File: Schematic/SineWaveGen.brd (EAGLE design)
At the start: 100 x 80 mm, 16 parts, among them IC1 MEGA32-P, Q1 G20N60, Q2 G20N60, Q3 H9NA80FI, Q4 H9NA80FI

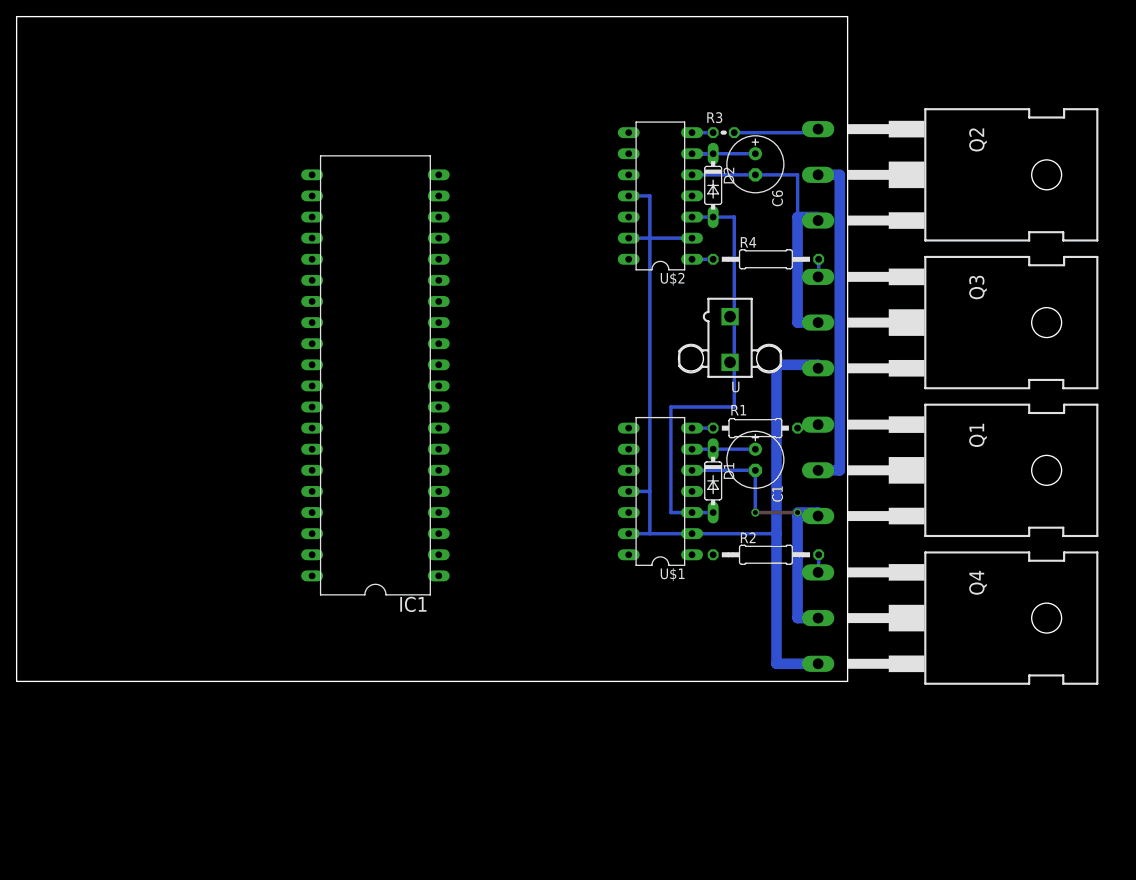
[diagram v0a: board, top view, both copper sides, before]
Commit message: use bigger distances for high voltages
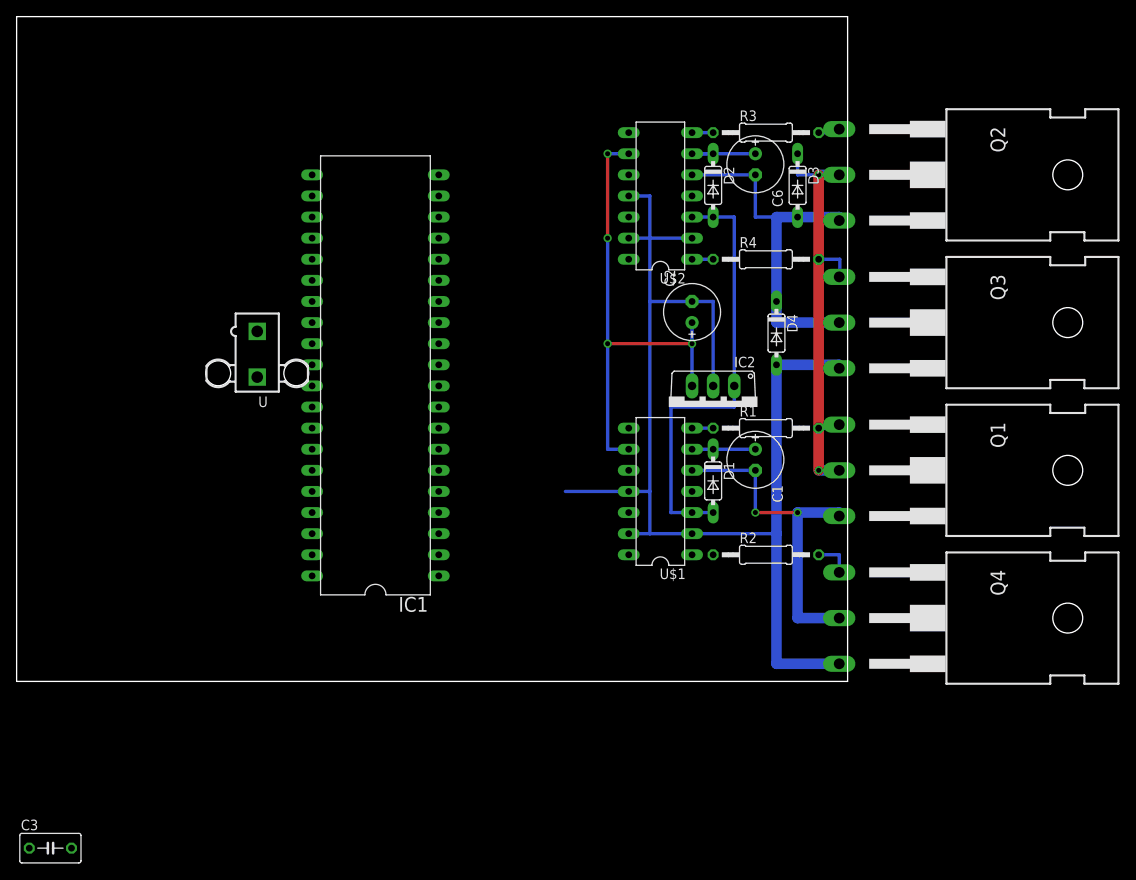
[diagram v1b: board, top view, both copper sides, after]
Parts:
- added C2: 100u, rcl:E2,5-7
- added C3: 100n, rcl:C050-035X075
- added D3, D4: 1N4148, diode:DO35-7
- added IC2: 7805TV, linear:TO220V
- Q1: value G20N60 -> (none)
- Q2: value G20N60 -> H9NA80FI
- Q4: value H9NA80FI -> (none)
- R1: device rcl:0207/10 -> rcl:0207/12
- R3: device rcl:0204V -> rcl:0207/12
- moved U 56.9 mm to (29.0, 39.4)
- moved R3 5.08 mm to (90.2, 66.0)
- moved Q1 2.54 mm to (126.5, 25.4)
- moved Q2 2.54 mm to (126.5, 61.0)
- moved Q3 2.54 mm to (126.5, 43.2)
- moved Q4 2.54 mm to (126.5, 7.62)
- moved R1 1.27 mm to (90.2, 30.5)
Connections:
- net +12V: now also IC2.1
- net +5V: now also C2.+, C3.1, IC2.3
- net GND: now also C2.-, C3.2, D4.A, IC2.2
- net N$10: now also IC1.17; no longer IC1.18
- net N$11: now also IC1.20; no longer IC1.17
- net N$2: now also IC1.18; no longer IC1.19
- net N$32: now also D3.A, D4.C
- net N$4: now also IC1.19; no longer IC1.20
- net V+: now also D3.C
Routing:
- net +5V: track 0.00 -> 58.4 mm, vias 0 -> 4
- net GND: track 117.5 -> 148.0 mm
- net N$32: track 35.8 -> 46.0 mm
- net N$29: track 10.5 -> 2.89 mm
- net V+: track 40.8 -> 45.6 mm, vias 0 -> 2
- net N$6: track 37.9 -> 40.9 mm
- net N$31: track 2.19 -> 4.73 mm
- net N$8: track 2.19 -> 4.59 mm

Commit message: Make it possible to choose a trapez generator
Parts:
- removed IC1: MEGA32-P, atmel:DIL40
- added C4: 100n, rcl:C050-035X075
- added C5, C7: 100u, rcl:E2,5-7
- added D5, D6: 1N4148, diode:DO35-7
- added IC3: MEGA8515-P, atmel:DIL40
- added SV1: (no value), con-lstb:MA03-1
- moved C3 103.6 mm to (68.6, 61.0), turned to 270 degrees
- moved C2 1.80 mm to (80.0, 43.2), turned to 180 degrees
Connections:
- new net N$12: IC3.29, U$2.12
- new net N$3: IC3.15, U$1.12
- net +12V: now also C5.+, C7.+
- net +5V: now also C4.1, IC3.40; no longer IC1.10, IC1.30
- net GND: now also C4.2, C5.-, C7.-, D5.A, IC3.20, SV1.1; no longer IC1.11, IC1.31
- net N$10: now also IC3.11, SV1.2; no longer IC1.17, U$1.12
- net N$11: now also IC3.10, SV1.3; no longer IC1.20, U$1.10
- net N$2: now also IC3.39, U$2.10; no longer IC1.18, U$2.12
- net N$4: now also IC3.25, U$1.10; no longer IC1.19, U$2.10
- net N$6: now also D5.C, D6.A
- net V+: now also D6.C
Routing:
- net GND: track 148.0 -> 237.3 mm
- net N$3: track 0.00 -> 45.7 mm
- net N$12: track 0.00 -> 27.9 mm
- net N$4: track 0.00 -> 7.62 mm
- net N$2: track 0.00 -> 7.62 mm
- net +5V: track 58.4 -> 63.5 mm
- net +12V: track 53.3 -> 55.9 mm
- net N$6: track 40.9 -> 43.5 mm
- net N$11: track 0.00 -> 2.54 mm
- net N$10: track 0.00 -> 2.54 mm
- net V+: track 45.6 -> 48.1 mm
